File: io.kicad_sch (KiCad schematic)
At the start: 75 parts, among them IC16 MC1489, IC19 MC1488, IC23 MC1489, IC24 82C711, X7 24MHz

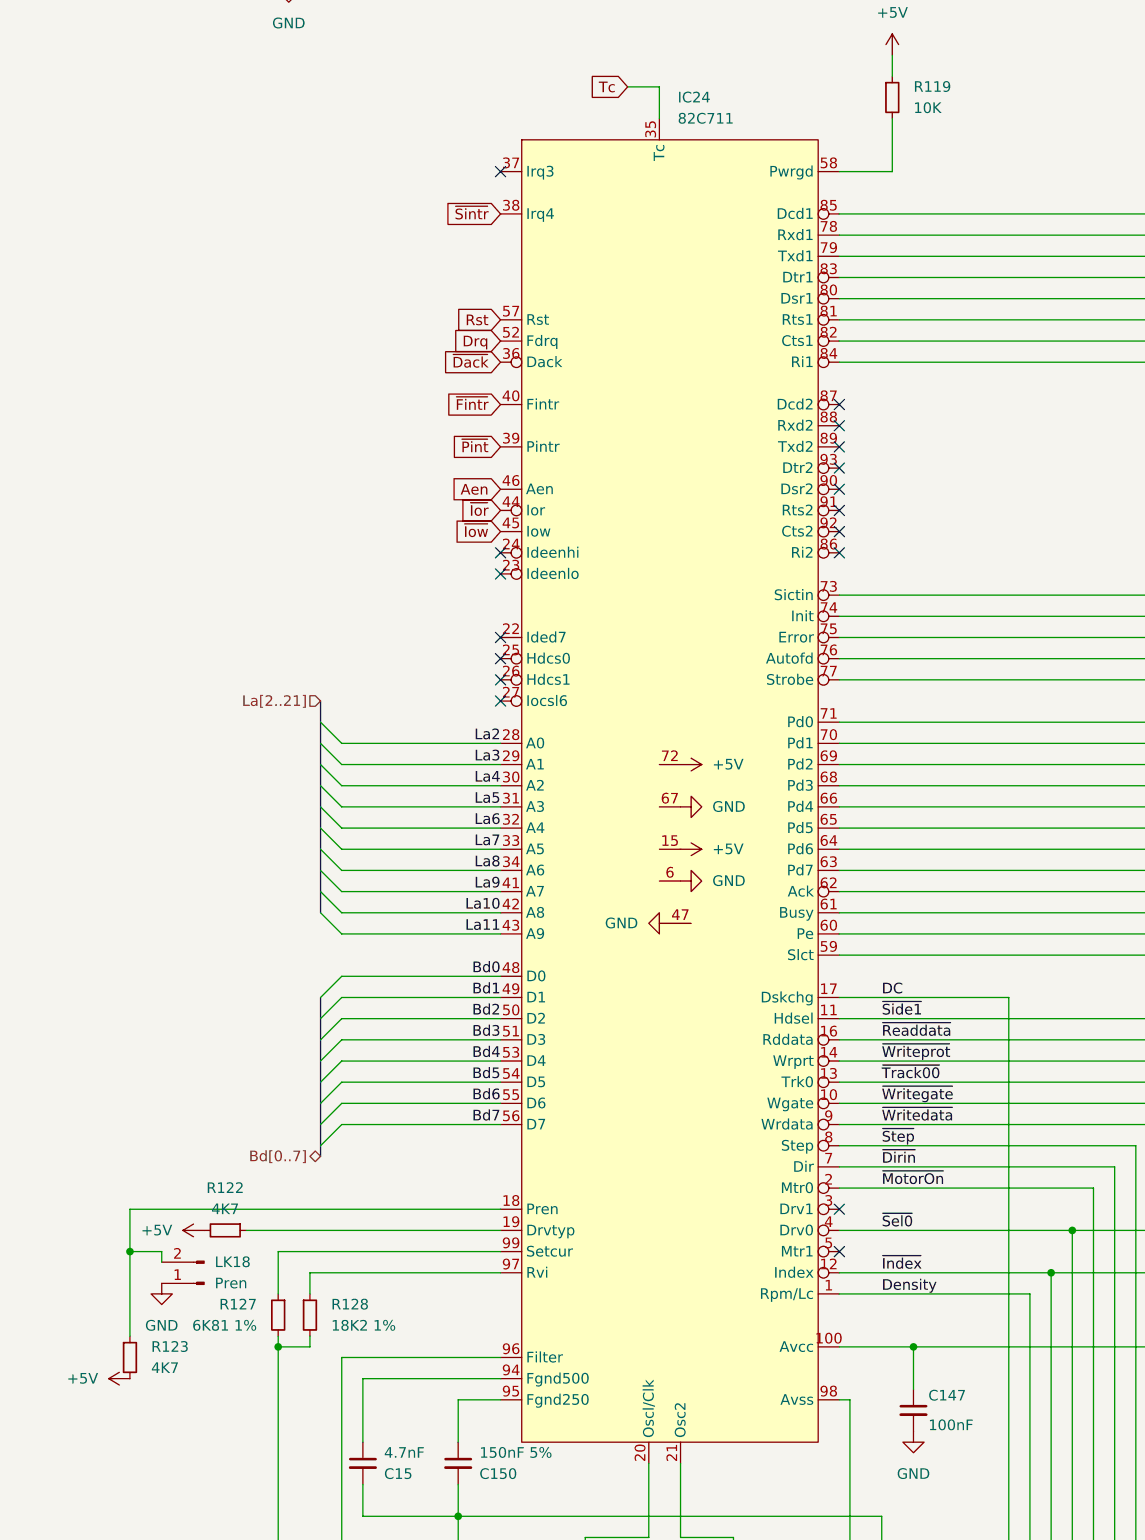
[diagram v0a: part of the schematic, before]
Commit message: adjust shielding perimeter trace and mounting holes
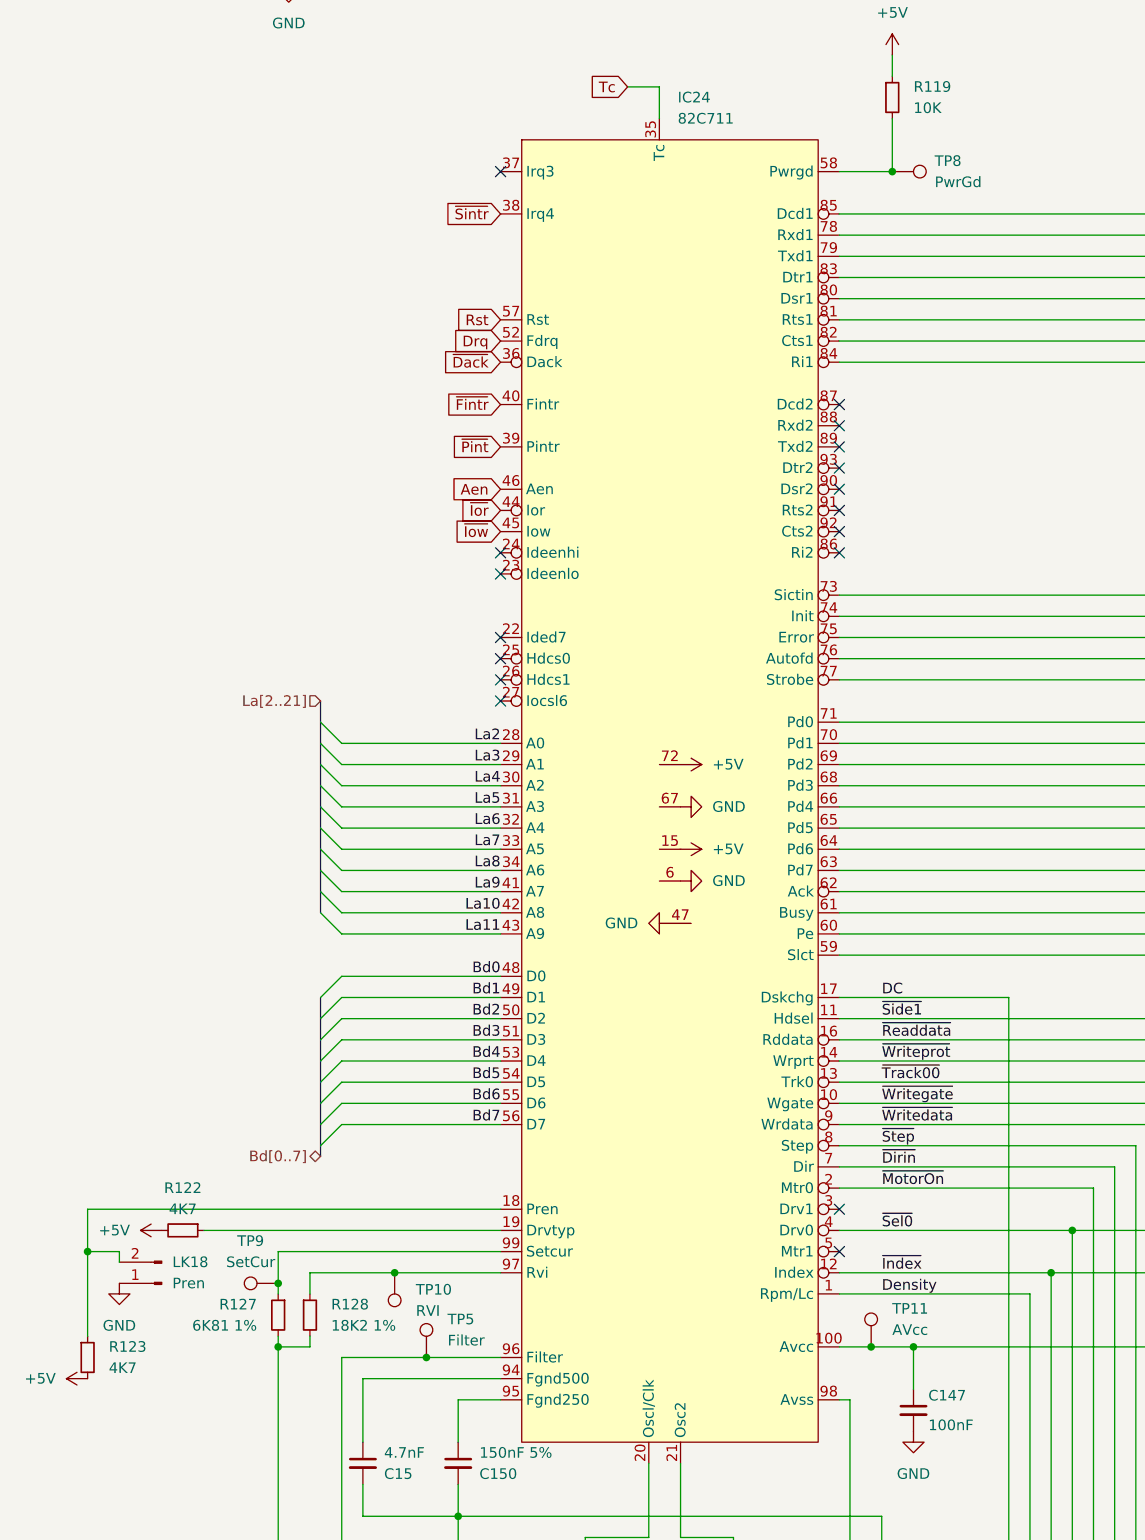
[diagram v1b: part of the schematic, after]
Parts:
- added TP10: RVI, TestPoint:TestPoint_Pad_D1.0mm, symbol Connector:TestPoint
- added TP11: AVcc, TestPoint:TestPoint_Pad_D1.0mm, symbol Connector:TestPoint
- added TP5: Filter, TestPoint:TestPoint_Pad_D1.0mm, symbol Connector:TestPoint
- added TP8: PwrGd, TestPoint:TestPoint_Pad_D1.0mm, symbol Connector:TestPoint
- added TP9: SetCur, TestPoint:TestPoint_Pad_D1.0mm, symbol Connector:TestPoint
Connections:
- net at C149.1, IC24.96 (Filter), R129.2: now also TP5.1
- net at IC24.97 (Rvi), R128.1: now also TP10.1
- net at IC24.99 (Setcur), R127.1: now also TP9.1
- net at C147.1, IC24.100 (Avcc), L14.1: now also TP11.1
- net at IC24.58 (Pwrgd), R119.2: now also TP8.1
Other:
- moved on the sheet: LK18, R122, R123

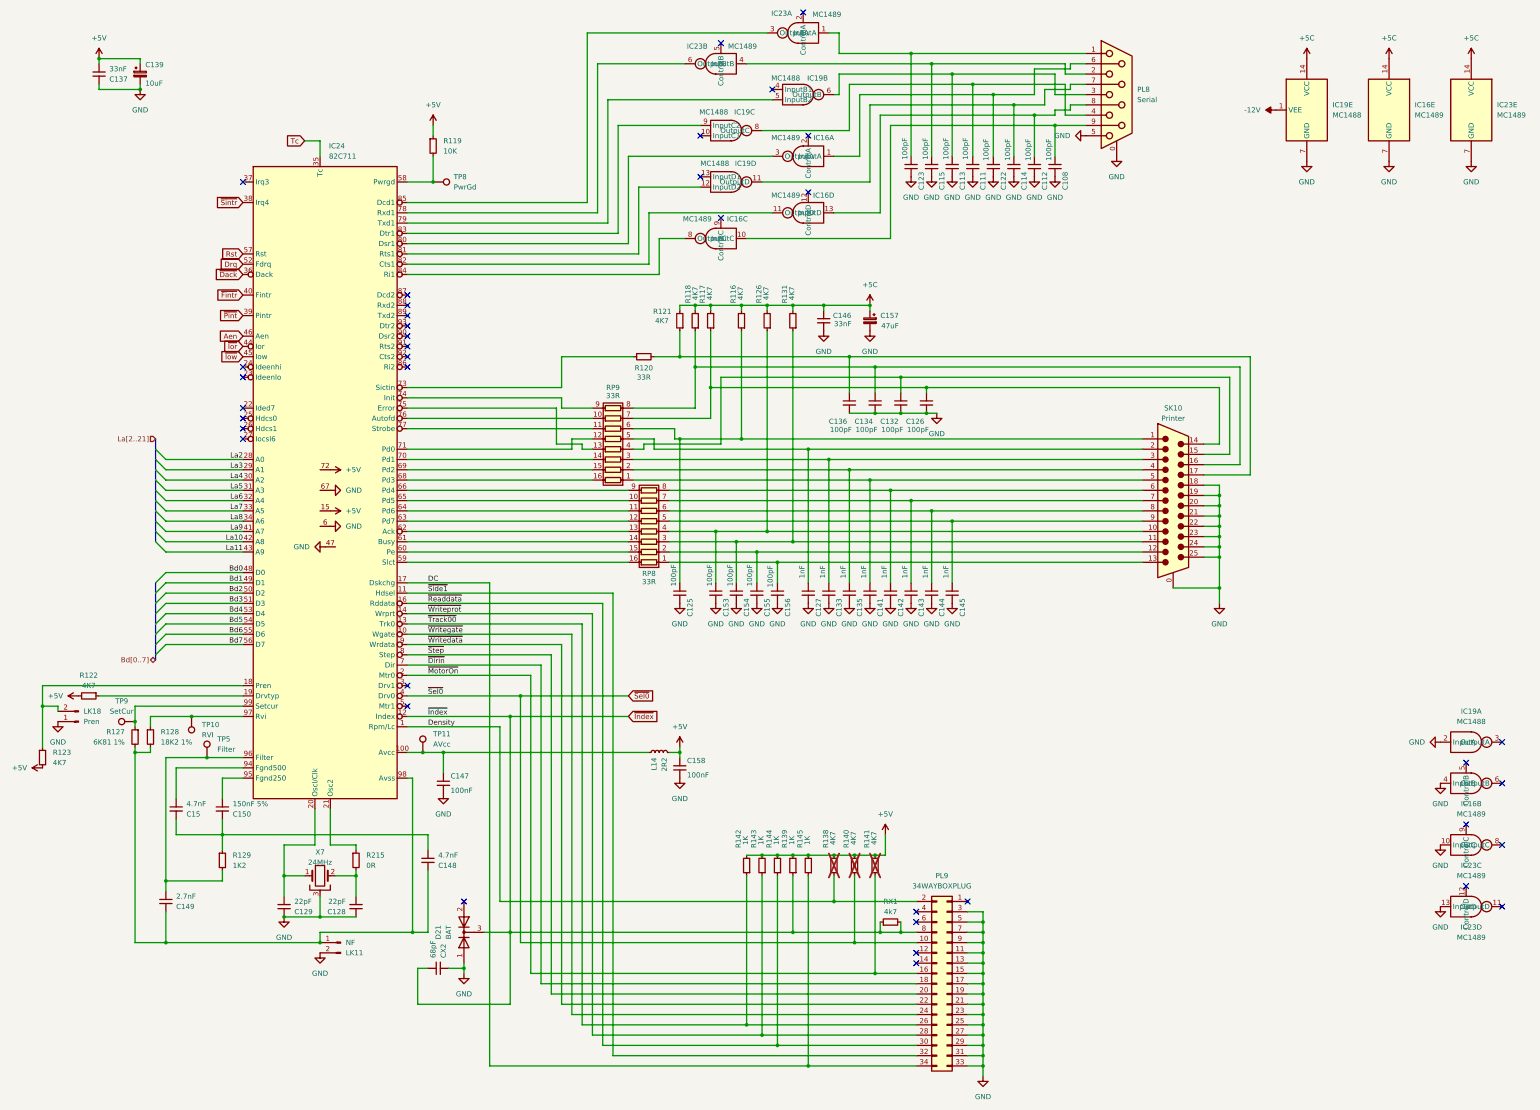
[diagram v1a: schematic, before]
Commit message: add ide and rework onboard ram
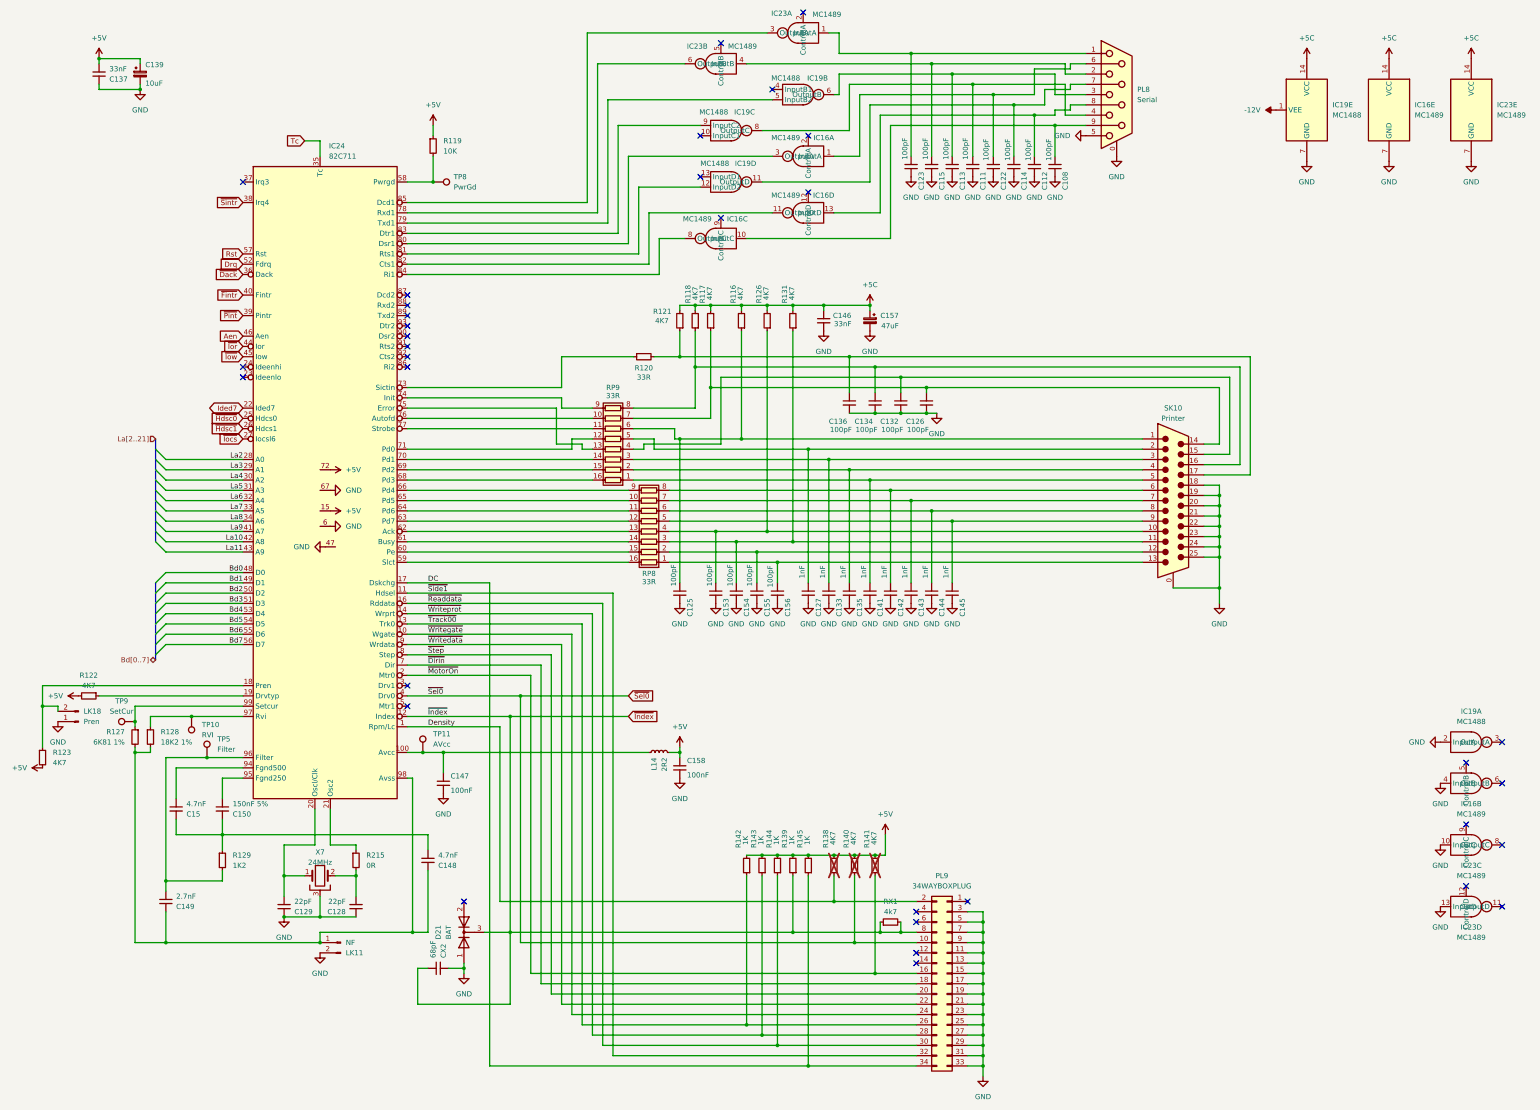
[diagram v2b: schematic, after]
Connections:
- net Ided7: now reaches IC24.22 (Ided7)
- net ~{Hdsc0}: now reaches IC24.25 (Hdcs0)
- net ~{Hdsc1}: now reaches IC24.26 (Hdcs1)
- net ~{Iocs}: now reaches IC24.27 (Iocsl6)
- no-connect marks 38 -> 34
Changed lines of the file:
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@@
 (kicad_sch
-	(version 20231120)
+	(version 20250114)
 	(generator "eeschema")
-	(generator_version "8.0")
+	(generator_version "9.0")
 	(paper "A3")
 	(title_block
@@
 	)
 	(no_connect
-		(at 87.63 120.65)
-	)
-	(no_connect
 		(at 398.78 220.98)
 	)
@@
 	)
 	(no_connect
-		(at 87.63 118.11)
-	)
-	(no_connect
 		(at 87.63 57.15)
 	)
@@
 	)
 	(no_connect
-		(at 87.63 113.03)
-	)
-	(no_connect
 		(at 227.33 59.69)
 	)
@@
 	)
 	(no_connect
-		(at 87.63 115.57)
-	)
-	(no_connect
 		(at 128.27 100.33)
 	)
@@
 		)
 	)
+	(global_label "~{Iocs}"
+		(shape input)
+		(at 87.63 120.65 180)
+		(fields_autoplaced yes)
+		(effects
+			(font
+				(size 1.27 1.27)
+			)
+			(justify right)
+		)
+		(property "Intersheetrefs" "${INTERSHEET_REFS}"
+			(at 80.7743 120.65 0)
+			(effects
+				(font
+					(size 1.27 1.27)
+				)
+				(justify right)
+				(hide yes)
+			)
+		)
+	)
 	(global_label "~{Pint}"
 		(shape input)
@@
 		)
 	)
+	(global_label "Ided7"
+		(shape bidirectional)
+		(at 87.63 113.03 180)
+		(fields_autoplaced yes)
+		(effects
+			(font
+				(size 1.27 1.27)
+			)
+			(justify right)
+		)
+		(property "Intersheetrefs" "${INTERSHEET_REFS}"
+			(at 78.3326 113.03 0)
+			(effects
+				(font
+					(size 1.27 1.27)
+				)
+				(justify right)
+				(hide yes)
+			)
+		)
+	)
 	(global_label "Tc"
 		(shape input)
@@
 		)
 	)
+	(global_label "~{Hdsc0}"
+		(shape input)
+		(at 87.63 115.57 180)
+		(fields_autoplaced yes)
+		(effects
+			(font
+				(size 1.27 1.27)
+			)
+			(justify right)
+		)
+		(property "Intersheetrefs" "${INTERSHEET_REFS}"
+			(at 78.8391 115.57 0)
+			(effects
+				(font
+					(size 1.27 1.27)
+				)
+				(justify right)
+				(hide yes)
+			)
+		)
+	)
 	(global_label "~{Iow}"
 		(shape input)
@@
 		)
 	)
+	(global_label "~{Hdsc1}"
+		(shape input)
+		(at 87.63 118.11 180)
+		(fields_autoplaced yes)
+		(effects
+			(font
+				(size 1.27 1.27)
+			)
+			(justify right)
+		)
+		(property "Intersheetrefs" "${INTERSHEET_REFS}"
+			(at 78.8391 118.11 0)
+			(effects
+				(font
+					(size 1.27 1.27)
+				)
+				(justify right)
+				(hide yes)
+			)
+		)
+	)
 	(hierarchical_label "Bd[0..7]"
 		(shape bidirectional)
@@
 		)
 		(instances
-			(project ""
+			(project "Acorn-A3010"
 				(path "/999882f3-94f8-4a89-9093-27a47d0cb289/b04534ef-c242-4ca8-9b8d-9d4b3e26f2f3"
 					(reference "IC16")
@@
 		)
 		(instances
-			(project ""
+			(project "Acorn-A3010"
 				(path "/999882f3-94f8-4a89-9093-27a47d0cb289/b04534ef-c242-4ca8-9b8d-9d4b3e26f2f3"
 					(reference "IC19")
@@
 		)
 		(instances
-			(project ""
+			(project "Acorn-A3010"
 				(path "/999882f3-94f8-4a89-9093-27a47d0cb289/b04534ef-c242-4ca8-9b8d-9d4b3e26f2f3"
 					(reference "PL9")
@@
 		)
 		(instances
-			(project ""
+			(project "Acorn-A3010"
 				(path "/999882f3-94f8-4a89-9093-27a47d0cb289/b04534ef-c242-4ca8-9b8d-9d4b3e26f2f3"
 					(reference "IC23")
@@
 		)
 		(instances
-			(project ""
+			(project "Acorn-A3010"
 				(path "/999882f3-94f8-4a89-9093-27a47d0cb289/b04534ef-c242-4ca8-9b8d-9d4b3e26f2f3"
 					(reference "IC16")
@@
 		)
 		(instances
-			(project ""
+			(project "Acorn-A3010"
 				(path "/999882f3-94f8-4a89-9093-27a47d0cb289/b04534ef-c242-4ca8-9b8d-9d4b3e26f2f3"
 					(reference "SK10")
@@
 		)
 		(instances
-			(project ""
+			(project "Acorn-A3010"
 				(path "/999882f3-94f8-4a89-9093-27a47d0cb289/b04534ef-c242-4ca8-9b8d-9d4b3e26f2f3"
 					(reference "IC16")
@@
 		)
 		(instances
-			(project ""
+			(project "Acorn-A3010"
 				(path "/999882f3-94f8-4a89-9093-27a47d0cb289/b04534ef-c242-4ca8-9b8d-9d4b3e26f2f3"
 					(reference "TP5")
@@
 		)
 		(instances
-			(project ""
+			(project "Acorn-A3010"
 				(path "/999882f3-94f8-4a89-9093-27a47d0cb289/b04534ef-c242-4ca8-9b8d-9d4b3e26f2f3"
 					(reference "IC19")
@@
 		)
 		(instances
-			(project ""
+			(project "Acorn-A3010"
 				(path "/999882f3-94f8-4a89-9093-27a47d0cb289/b04534ef-c242-4ca8-9b8d-9d4b3e26f2f3"
 					(reference "IC19")
@@
 		)
 		(instances
-			(project ""
+			(project "Acorn-A3010"
 				(path "/999882f3-94f8-4a89-9093-27a47d0cb289/b04534ef-c242-4ca8-9b8d-9d4b3e26f2f3"
 					(reference "IC23")
@@
 		)
 		(instances
-			(project ""
+			(project "Acorn-A3010"
 				(path "/999882f3-94f8-4a89-9093-27a47d0cb289/b04534ef-c242-4ca8-9b8d-9d4b3e26f2f3"
 					(reference "IC16")
@@
 		)
 		(instances
-			(project ""
+			(project "Acorn-A3010"
 				(path "/999882f3-94f8-4a89-9093-27a47d0cb289/b04534ef-c242-4ca8-9b8d-9d4b3e26f2f3"
 					(reference "IC23")
@@
 		)
 		(instances
-			(project ""
+			(project "Acorn-A3010"
 				(path "/999882f3-94f8-4a89-9093-27a47d0cb289/b04534ef-c242-4ca8-9b8d-9d4b3e26f2f3"
 					(reference "IC24")
@@
 		)
 		(instances
-			(project ""
+			(project "Acorn-A3010"
 				(path "/999882f3-94f8-4a89-9093-27a47d0cb289/b04534ef-c242-4ca8-9b8d-9d4b3e26f2f3"
 					(reference "IC23")
@@
 		)
 		(instances
-			(project ""
+			(project "Acorn-A3010"
 				(path "/999882f3-94f8-4a89-9093-27a47d0cb289/b04534ef-c242-4ca8-9b8d-9d4b3e26f2f3"
 					(reference "LK18")
@@
 		)
 		(instances
-			(project ""
+			(project "Acorn-A3010"
 				(path "/999882f3-94f8-4a89-9093-27a47d0cb289/b04534ef-c242-4ca8-9b8d-9d4b3e26f2f3"
 					(reference "IC19")
@@
 		)
 		(instances
-			(project ""
+			(project "Acorn-A3010"
 				(path "/999882f3-94f8-4a89-9093-27a47d0cb289/b04534ef-c242-4ca8-9b8d-9d4b3e26f2f3"
 					(reference "IC16")
@@
 		)
 		(instances
-			(project ""
+			(project "Acorn-A3010"
 				(path "/999882f3-94f8-4a89-9093-27a47d0cb289/b04534ef-c242-4ca8-9b8d-9d4b3e26f2f3"
 					(reference "IC23")
@@
 		)
 		(instances
-			(project ""
+			(project "Acorn-A3010"
 				(path "/999882f3-94f8-4a89-9093-27a47d0cb289/b04534ef-c242-4ca8-9b8d-9d4b3e26f2f3"
 					(reference "#PWR0274")
@@
 		)
 		(instances
-			(project ""
+			(project "Acorn-A3010"
 				(path "/999882f3-94f8-4a89-9093-27a47d0cb289/b04534ef-c242-4ca8-9b8d-9d4b3e26f2f3"
 					(reference "IC19")
